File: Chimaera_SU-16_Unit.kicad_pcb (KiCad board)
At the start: 2 copper layers, 80 x 30 mm, 65 parts, among them P0 CONN_4, P1 CONN_4, P2 CONN_3, U0 CD74HC4067, U1 MCP602, U2 MCP1703

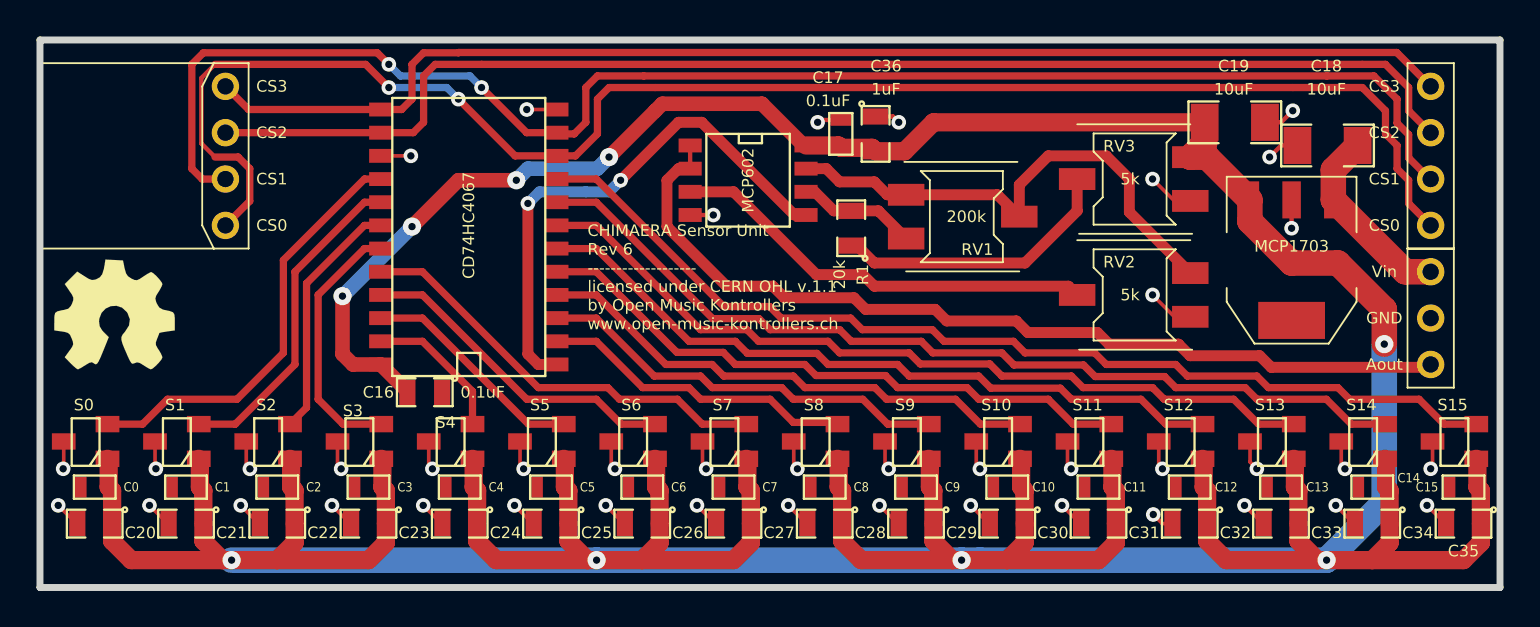
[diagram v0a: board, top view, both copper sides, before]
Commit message: DSP-F3 rev3 (+1 analog input) and SU-16 rev7 (reverse current diode), Hershey fonts for case side
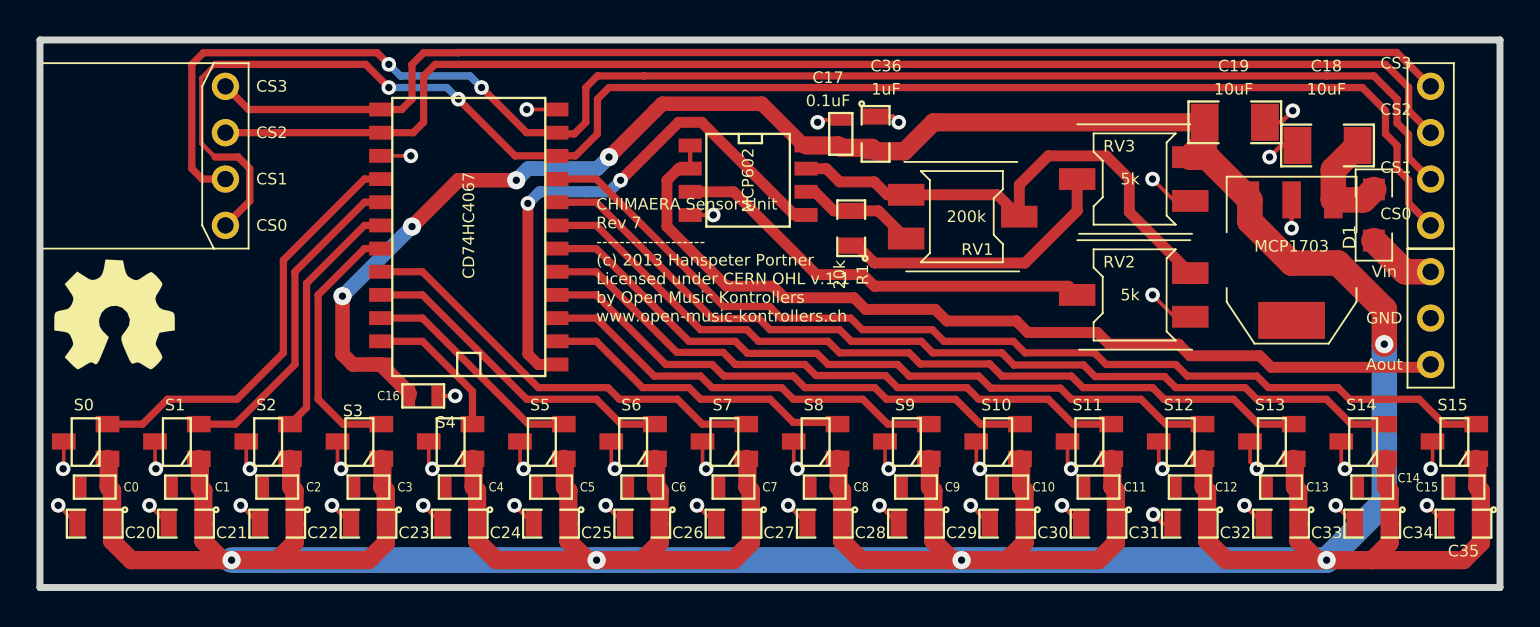
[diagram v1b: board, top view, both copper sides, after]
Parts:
- added D1: DIODE, SOD123W, F.Cu at (85.1, 21.6)
- C16: footprint SM0805 -> SM0603
- moved C16 0.21 mm to (33.0, 31.5)
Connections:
- C18 pad 1: Vdd -> N-0000015
- U2 pad 1: Vdd -> N-0000015
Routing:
- net Vdd: track 10.5 -> 3.82 mm
- net N-0000015: track 0.00 -> 5.99 mm
- net GND: track 66.0 -> 66.9 mm, vias 42 -> 43
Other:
- board text added: "CHIMAERA Sensor Unit Rev 7 ------------------- (c) 2013 Hanspeter Portner Licensed under CERN OHL v.1.1 by Open Music Kontrollers www.open-music-kontrollers.ch"
- board text removed: "CHIMAERA Sensor Unit Rev 6 ------------------- licensed under CERN OHL v.1.1 by Open Music Kontrollers www.open-music-kontrollers.ch"

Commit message: last changes for Alpha Batch PCBs
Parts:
- added C37: 1uF, SM0805, F.Cu at (33.3, 31.6)
- moved C16 2.71 mm to (30.3, 31.4), turned to 0 degrees
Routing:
- net GND: track 66.9 -> 68.6 mm, vias 43 -> 44
- net Vcc: track 302.4 -> 303.2 mm
